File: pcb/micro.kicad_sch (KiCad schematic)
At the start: 26 parts, among them J2 DBG, SW1 BOOT, SW2 RST, U1 RP2040, U5 W25Q128JVSIQ, Y1 12MHz

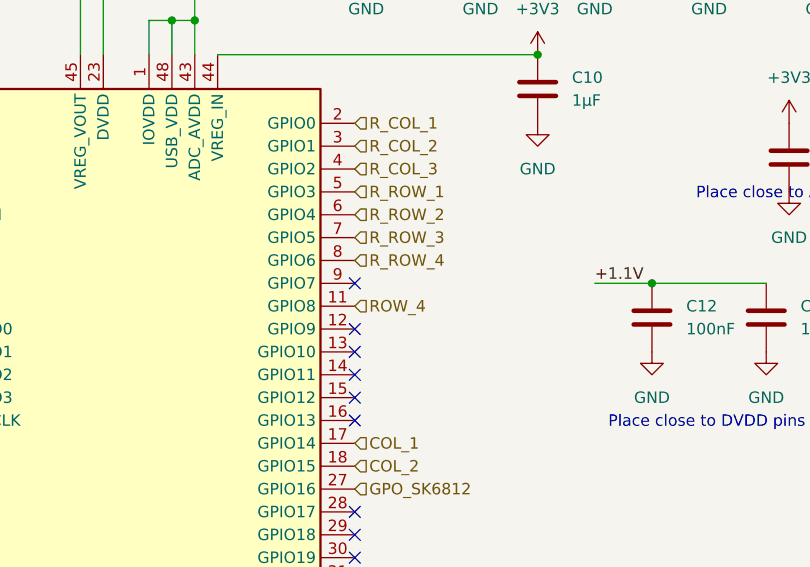
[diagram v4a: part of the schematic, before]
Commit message: Placing more components onto the PCB and removing more stale leftovers from the now absent Rotary Encoder.
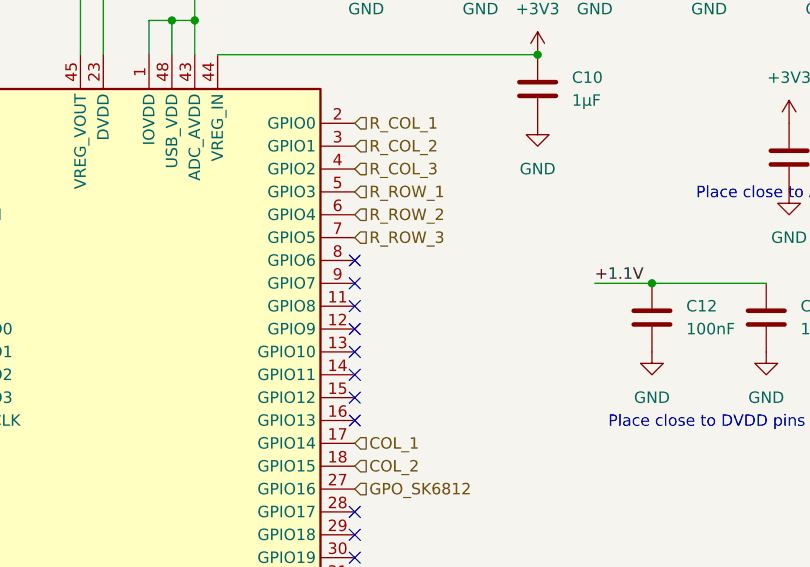
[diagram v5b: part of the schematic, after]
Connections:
- net ROW_4: no longer names the net of U1.11 (GPIO8)
- net R_ROW_4: no longer names the net of U1.8 (GPIO6)
- no-connect marks 17 -> 19
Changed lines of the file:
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@@
+	)
+	(no_connect
+		(at 177.8 74.93)
 	)
 	(no_connect
@@
 	(no_connect
 		(at 177.8 80.01)
+	)
+	(no_connect
+		(at 177.8 69.85)
 	)
 	(no_connect
@@
 		)
 	)
-	(hierarchical_label "R_ROW_4"
-		(shape input)
-		(at 177.8 69.85 0)
-		(fields_autoplaced yes)
-		(effects
-			(font
-				(size 1.27 1.27)
-			)
-			(justify left)
-		)
-	)
 	(hierarchical_label "COL_1"
 		(shape input)
@@
 		(fields_autoplaced yes)
 		(effects
-			(font
-				(size 1.27 1.27)
-			)
-			(justify left)
-		)
-	)
-	(hierarchical_label "ROW_4"
-		(shape input)
-		(at 177.8 74.93 0)
-		(fields_autoplaced yes)
-		(effects

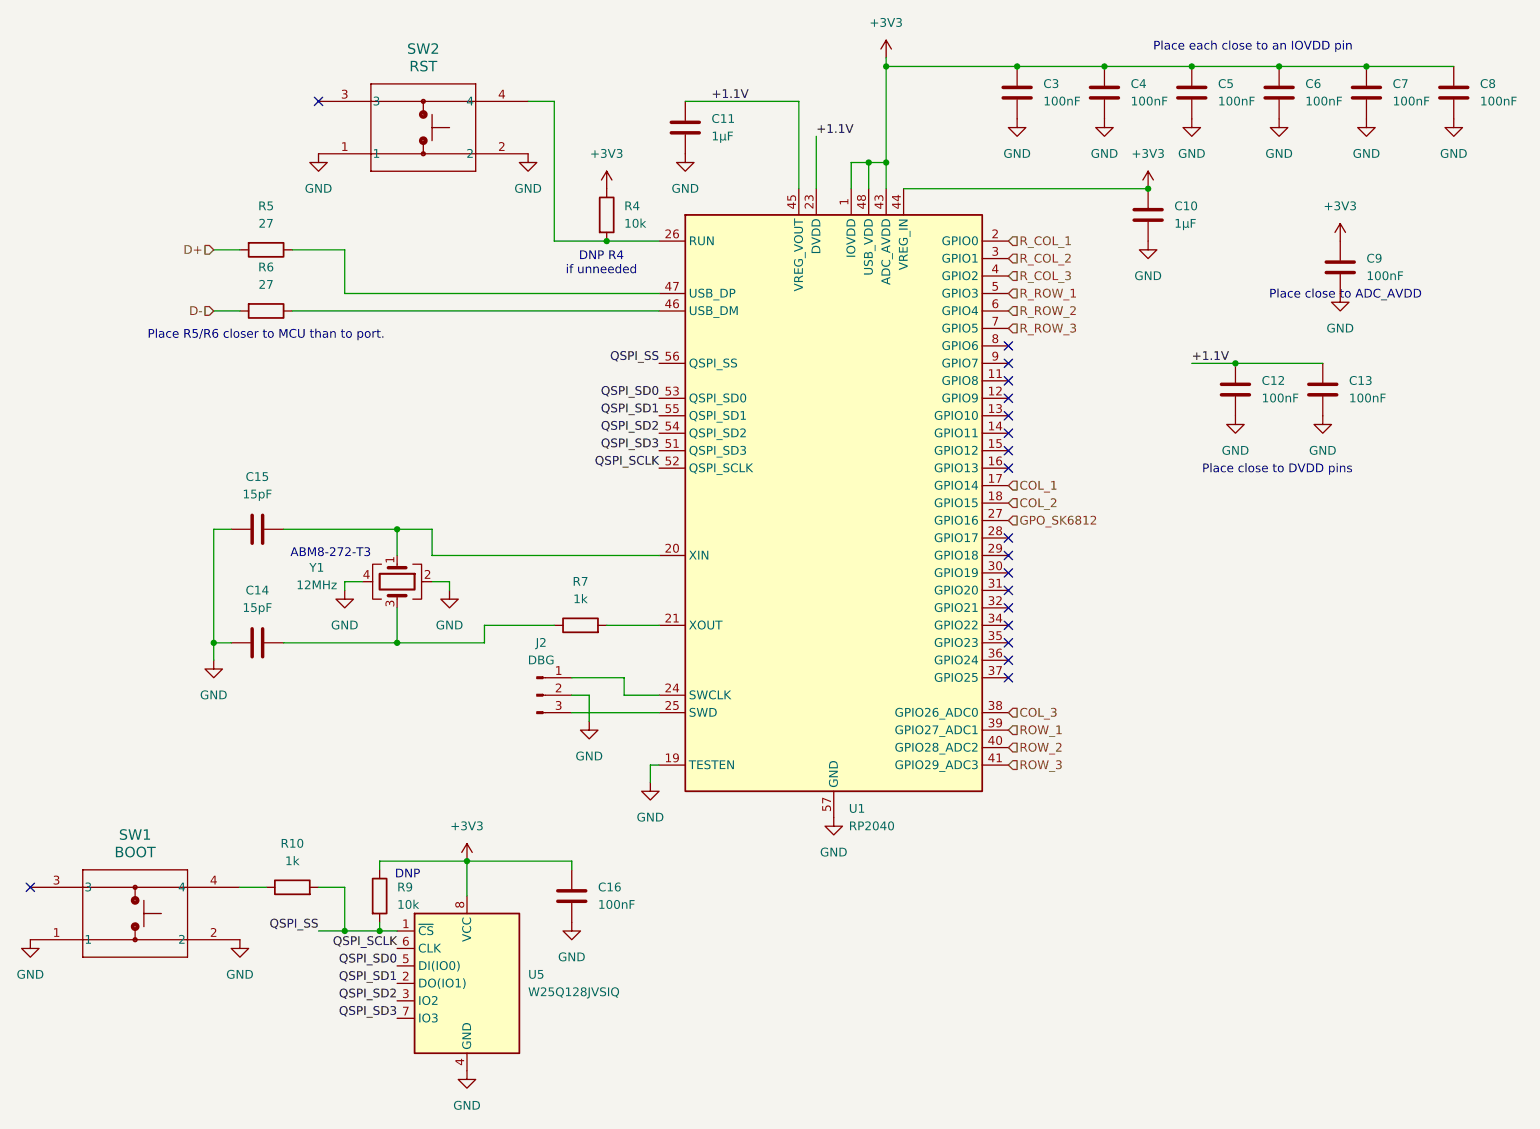
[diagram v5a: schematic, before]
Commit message: WIP: Starting to migrate toward 2 independant halves.
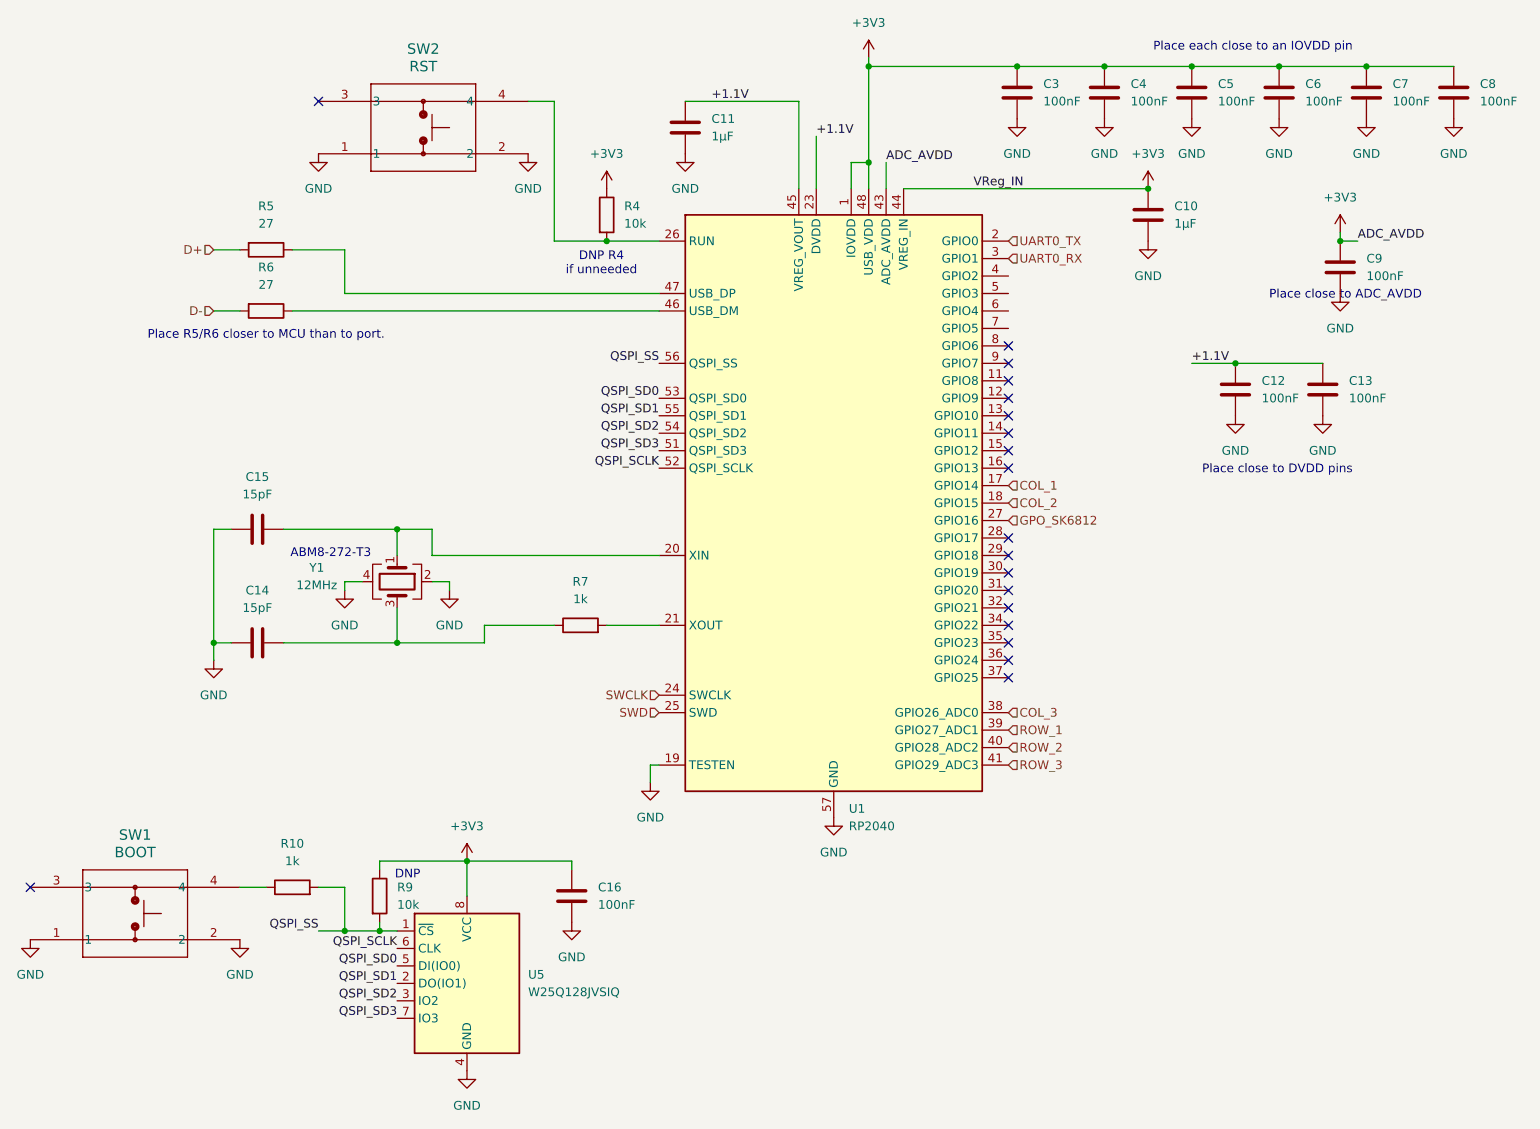
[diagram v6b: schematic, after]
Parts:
- removed J2: DBG, Connector_PinHeader_2.54mm:PinHeader_1x03_P2.54mm_Vertical, symbol Connector:Conn_01x03_Pin
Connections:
- net SWCLK: now reaches U1.24 (SWCLK)
- net SWD: now reaches U1.25 (SWD)
- net R_COL_1 renamed UART0_TX
- net R_COL_2 renamed UART0_RX
- net R_COL_3: no longer names the net of U1.4 (GPIO2)
- net R_ROW_1: no longer names the net of U1.5 (GPIO3)
- net R_ROW_2: no longer names the net of U1.6 (GPIO4)
- net R_ROW_3: no longer names the net of U1.7 (GPIO5)

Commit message: WIP: Updating keyboard matrix to use the new shared part and reorganizing all the LED outputs.
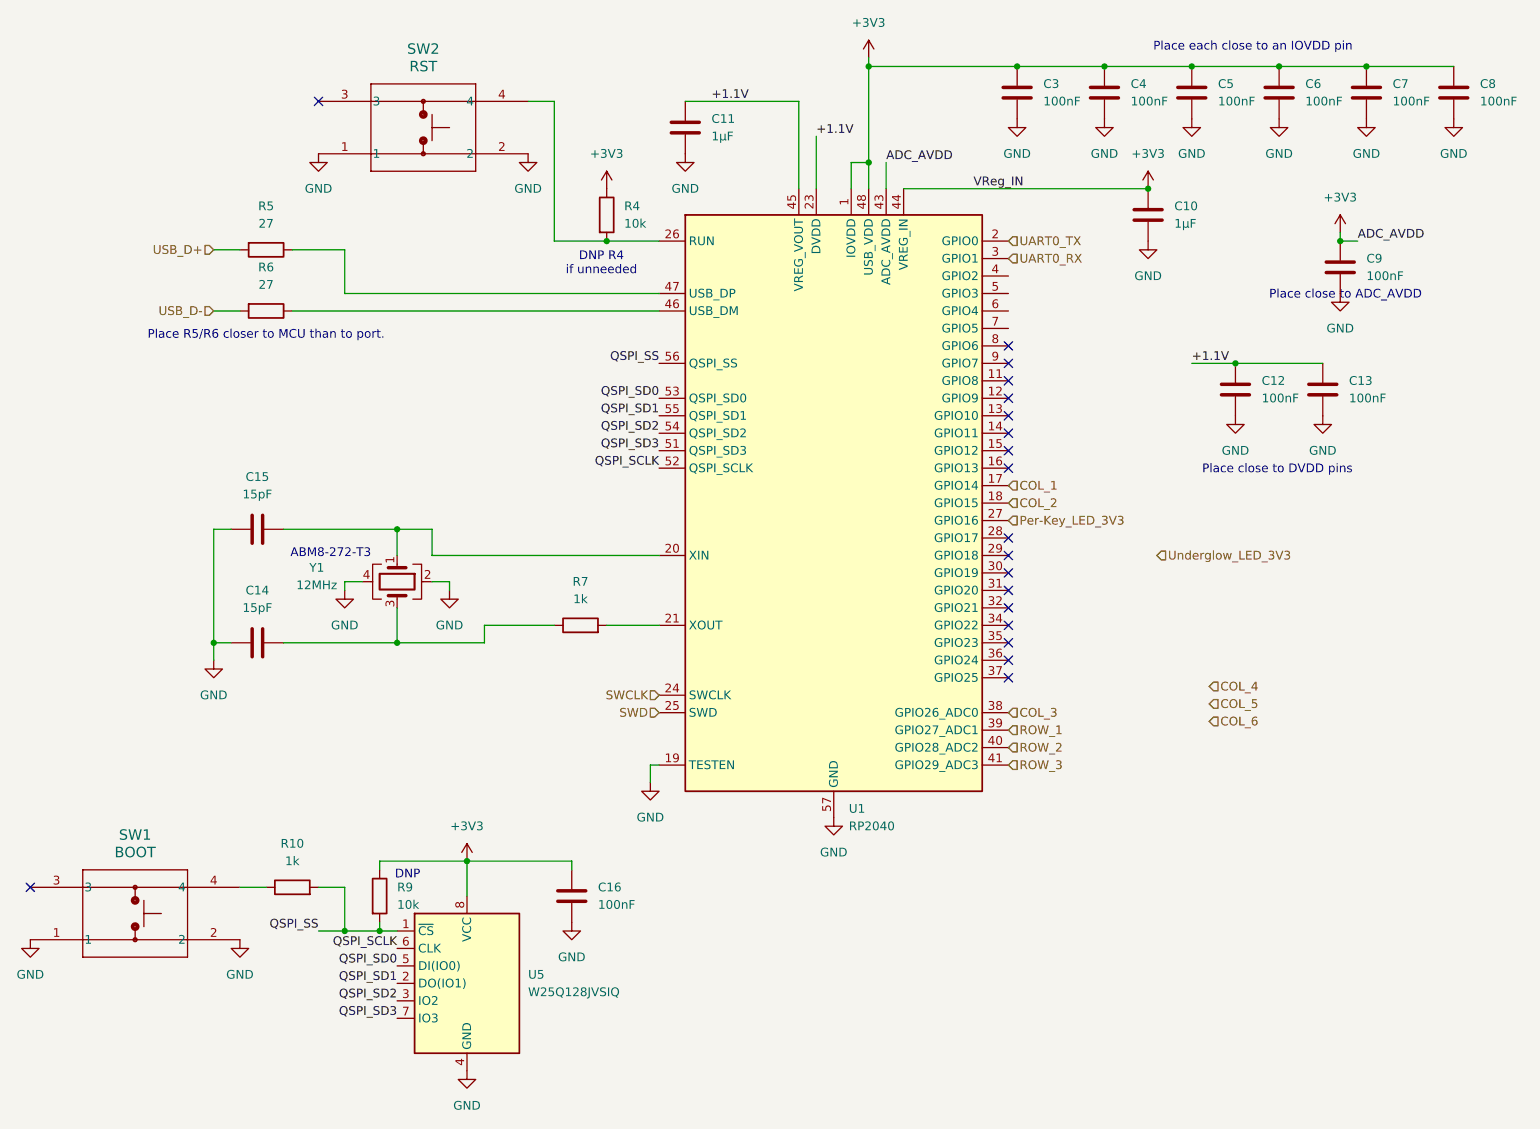
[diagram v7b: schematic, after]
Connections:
- net D+ renamed USB_D+
- net D- renamed USB_D-
- net GPO_SK6812 renamed Per-Key_LED_3V3
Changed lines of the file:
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@@
 		)
 	)
-	(hierarchical_label "D-"
+	(hierarchical_label "USB_D-"
 		(shape input)
 		(at 62.23 64.77 180)
@@
 		)
 	)
-	(hierarchical_label "D+"
+	(hierarchical_label "USB_D+"
 		(shape input)
 		(at 62.23 55.88 180)
@@
 			)
 			(justify right)
+		)
+	)
+	(hierarchical_label "COL_4"
+		(shape input)
+		(at 207.01 119.38 0)
+		(fields_autoplaced yes)
+		(effects
+			(font
+				(size 1.27 1.27)
+			)
+			(justify left)
 		)
 	)
@@
 		(shape input)
 		(at 177.8 130.81 0)
+		(fields_autoplaced yes)
+		(effects
+			(font
+				(size 1.27 1.27)
+			)
+			(justify left)
+		)
+	)
+	(hierarchical_label "COL_5"
+		(shape input)
+		(at 207.01 121.92 0)
 		(fields_autoplaced yes)
 		(effects
@@
 		)
 	)
-	(hierarchical_label "GPO_SK6812"
+	(hierarchical_label "Underglow_LED_3V3"
+		(shape input)
+		(at 199.39 100.33 0)
+		(fields_autoplaced yes)
+		(effects
+			(font
+				(size 1.27 1.27)
+			)
+			(justify left)
+		)
+	)
+	(hierarchical_label "COL_6"
+		(shape input)
+		(at 207.01 124.46 0)
+		(fields_autoplaced yes)
+		(effects
+			(font
+				(size 1.27 1.27)
+			)
+			(justify left)
+		)
+	)
+	(hierarchical_label "Per-Key_LED_3V3"
 		(shape input)
 		(at 177.8 95.25 0)
